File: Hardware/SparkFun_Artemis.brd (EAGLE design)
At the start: 15 x 10 mm, 74 parts, among them J1 PAD.4X.6, J10 PAD.4X.6, J11 PAD.4X.6, J12 PAD.4X.6, J13 PAD.4X.6, J14 PAD.4X.6, J15 PAD.4X.6, J16 PAD.4X.6, J17 PAD.4X.6, J18 PAD.4X.6, J19 PAD.4X.6, J2 PAD.4X.6, J20 PAD.4X.6, J21 PAD.4X.6, J22 PAD.4X.6, J23 PAD.4X.6, J24 PAD.4X.6, J25 PAD.4X.6, J26 PAD.4X.6, J27 PAD.4X.6, J28 PAD.4X.6, J29 PAD.4X.6, J3 PAD.4X.6, J30 PAD.4X.6, J31 PAD.4X.6, J32 PAD.4X.6, J34 PAD.4X.6, J35 PAD.4X.6, J36 PAD.4X.6, J37 PAD.4X.6, J38 PAD.4X.6, J39 PAD.4X.6, J4 PAD.4X.6, J40 PAD.4X.6, J41 PAD.4X.6, J42 PAD.4X.6, J43 PAD.4X.6, J44 PAD.4X.6, J45 PAD.4X.6, J46 PAD.35X.35, J47 PAD.4X.6, J48 PAD.4X.6, J49 PAD.4X.6, J5 PAD.4X.6, J6 PAD.4X.6, J7 PAD.4X.6, J8 PAD.4X.6, J9 PAD.4X.6, U1 AMBIQ-APOLLO3KBR, Y1 32MHz

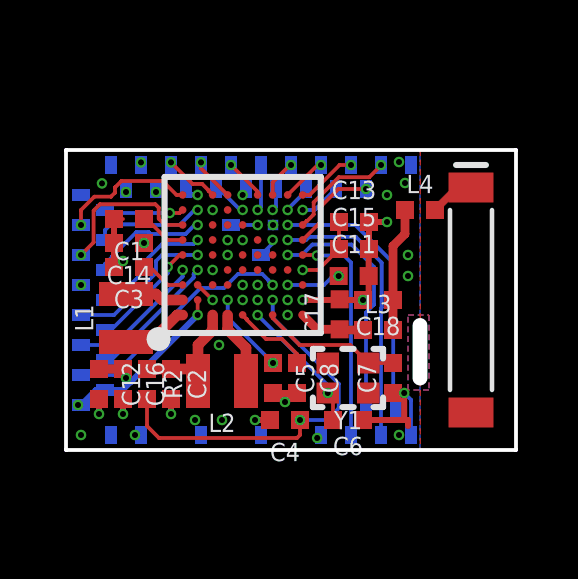
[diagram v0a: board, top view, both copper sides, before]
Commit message: Going to buried vias
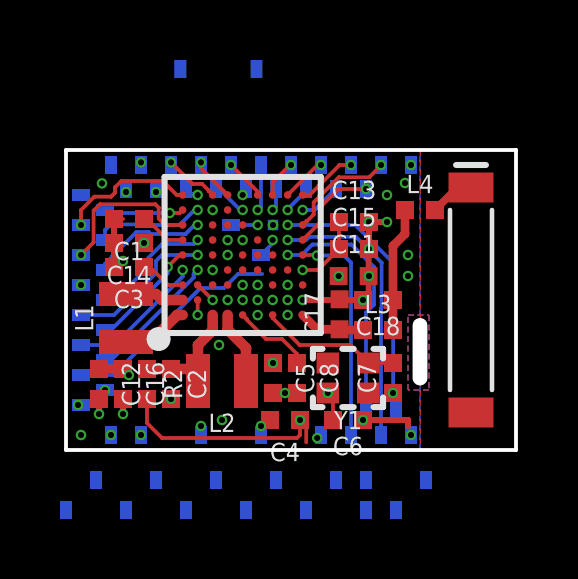
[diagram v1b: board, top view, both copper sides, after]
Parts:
- added J33, J50, J51, J52, J56, J57, J58, J59, J60, J61, J62, J63, J64, J65, J66, J67: PAD.4X.6, Module-Pads:MODULE_PAD
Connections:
- new net D0: J33.1, U1.H4
- new net D1: J50.1, U1.G4
- new net D14: J56.1, U1.D7
- new net D15: J57.1, U1.C7
- new net D16: J58.1, U1.D4
- new net D17: J59.1, U1.D3
- new net D18: J60.1, U1.C5
- new net D19: J61.1, U1.C3
- new net D2: J51.1, U1.F4
- new net D23: J62.1, U1.D8
- new net D3: J52.1, U1.G5
- new net D30: J63.1, U1.F6
- new net D34: J64.1, U1.C6
- new net D41: J65.1, U1.E5
- new net D45: J66.1, U1.F5
- new net D46: J67.1, U1.E7
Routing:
- net VDD: track 9.78 -> 4.13 mm, vias 7 -> 8
- net GND: track 15.7 -> 11.6 mm, vias 29 -> 34
- net VDCDCRF: track 12.7 -> 13.4 mm
- net N$3: track 4.84 -> 4.29 mm
- net !RST: track 7.96 -> 7.45 mm, vias 1 -> 0

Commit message: Buried via approach. Moar GPIOs!
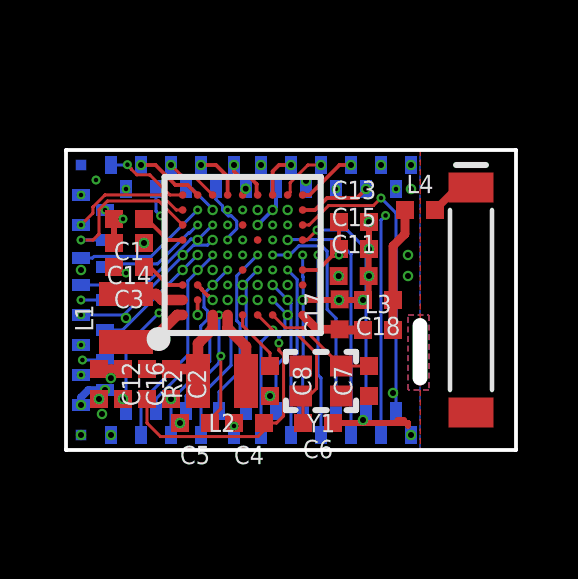
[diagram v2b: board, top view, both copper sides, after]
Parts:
- removed J34, J47, J48, J63, J67: PAD.4X.6, Module-Pads:MODULE_PAD
- J27, J44: value PAD.4X.6 -> PAD.35X.35; device Module-Pads:MODULE_PAD -> Module-Pads:MODULE_MINI_PAD
- J46: value PAD.35X.35 -> PAD.4X.6; device Module-Pads:MODULE_MINI_PAD -> Module-Pads:MODULE_PAD
- moved J56 11.4 mm to (2.00, 8.70), turned to 90 degrees
- moved J23 8.22 mm to (11.0, 1.30)
- moved J44 8.00 mm to (0.50, 0.50)
- moved J57 7.52 mm to (0.50, 5.50), turned to 0 degrees
- moved J36 7.40 mm to (10.0, 1.30)
- moved J30 6.61 mm to (7.00, 1.30), turned to 90 degrees
- moved J64 5.52 mm to (0.50, 4.50), turned to 180 degrees
- moved J4 5.47 mm to (4.00, 1.30), turned to 90 degrees
- moved J2 5.01 mm to (11.0, 8.70), turned to 270 degrees
- moved J33 4.74 mm to (7.50, 0.50)
- moved J66 4.53 mm to (5.10, 1.30)
- moved J18 4.50 mm to (0.50, 8.50), turned to 180 degrees
- moved J26 4.10 mm to (5.60, 0.50)
- moved J62 4.08 mm to (3.00, 8.70), turned to 90 degrees
- moved J51 3.86 mm to (6.00, 1.30)
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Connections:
- removed net D30: J63.1, U1.F6
- removed net D46: J67.1, U1.E7
- net GND: no longer J34.1, J47.1, J48.1
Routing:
- net D3: track 0.00 -> 7.46 mm, vias 0 -> 1
- net D18: track 0.00 -> 6.99 mm, vias 0 -> 1
- net D41: track 0.00 -> 6.58 mm, vias 0 -> 2
- net ~D44: track 3.74 -> 10.3 mm
- net SWDCK: track 0.66 -> 7.05 mm, vias 1 -> 2
- net D45: track 0.00 -> 5.97 mm, vias 0 -> 1
- net D1: track 0.00 -> 5.96 mm, vias 0 -> 2
- net D17: track 0.00 -> 5.94 mm, vias 0 -> 2
- net D19: track 0.00 -> 5.91 mm, vias 0 -> 2
- net D16: track 0.00 -> 5.79 mm, vias 0 -> 1
- net D0: track 0.00 -> 5.72 mm, vias 0 -> 1
- net D34: track 0.00 -> 5.42 mm, vias 0 -> 2
- net D15: track 0.00 -> 5.22 mm, vias 0 -> 1
- net ~D6: track 1.20 -> 6.25 mm, vias 1 -> 2
- net D2: track 0.00 -> 4.86 mm, vias 0 -> 1
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
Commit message: Commit for Quote
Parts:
- removed J60, J61, J62, J64, J65, J66: PAD.4X.6, Module-Pads:MODULE_PAD
- added J34, J47, J48, J53, J54, J55: PAD.4X.6, Module-Pads:MODULE_PAD
- J22, J38: value PAD.4X.6 -> PAD.35X.35; device Module-Pads:MODULE_PAD -> Module-Pads:MODULE_MINI_PAD
- J27, J44: value PAD.35X.35 -> PAD.4X.6; device Module-Pads:MODULE_MINI_PAD -> Module-Pads:MODULE_PAD
- moved J25 13.0 mm to (0.50, 7.50), turned to 0 degrees
- moved J23 12.7 mm to (0.50, 8.50), turned to 180 degrees
- moved J57 11.2 mm to (10.5, 0.50), turned to 270 degrees
- moved J56 10.9 mm to (10.0, 1.30), turned to 270 degrees
- moved J32 10.7 mm to (1.30, 4.00), turned to 0 degrees
- moved J24 10.3 mm to (1.30, 8.00), turned to 0 degrees
- moved J9 9.90 mm to (7.50, 9.50), turned to 90 degrees
- moved J5 9.87 mm to (9.50, 9.50), turned to 270 degrees
- moved J4 9.53 mm to (10.0, 8.70), turned to 270 degrees
- moved J43 9.35 mm to (3.50, 0.50)
- moved J41 9.22 mm to (2.50, 0.50)
- moved J22 9.00 mm to (0.50, 9.50), turned to 90 degrees
- moved J38 9.00 mm to (0.50, 0.50), turned to 0 degrees
- moved J39 9.00 mm to (1.50, 0.50), turned to 90 degrees
- moved J42 8.92 mm to (3.00, 1.30)
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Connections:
- net !RST: now also J50.1; no longer J30.1
- net BOOTLOAD: now also J7.1; no longer J3.1
- net D0: now also J51.1; no longer J33.1
- net D1: now also J49.1; no longer J50.1
- net D10: now also J8.1; no longer J43.1
- net D14: now also J20.1; no longer J56.1
- net D15: now also J29.1; no longer J57.1
- net D16: now also J42.1; no longer J58.1
- net D17: now also J43.1; no longer J59.1
- net D18: now also J41.1; no longer J60.1
- net D19: now also J40.1; no longer J61.1
- net D2: now also J48.1; no longer J51.1
- net D23: now also J18.1; no longer J62.1
- net D3: now also J54.1; no longer J52.1
- net D34: now also J31.1; no longer J64.1
- net D36: now also J55.1; no longer J38.1
- net D38: now also J56.1; no longer J36.1
- net D40: now also J5.1; no longer J22.1
- net D41: now also J45.1; no longer J65.1
- net D45: now also J46.1; no longer J66.1
- net D7: now also J13.1; no longer J19.1
- net D8: now also J11.1; no longer J42.1
- net D9: now also J6.1; no longer J46.1
- net GND: now also J1.1, J22.1, J38.1, J39.1, J47.1, J59.1; no longer J24.1, J25.1, J26.1, J27.1, J44.1, J45.1
- net RXI-0: now also J3.1; no longer J32.1
- net SWDIO: now also J10.1; no longer J1.1
- net TXO-0: now also J9.1; no longer J31.1
- net VDD: now also J36.1, J37.1; no longer J29.1, J49.1
- net XI: now also J35.1; no longer J9.1
- net XO: now also J34.1; no longer J10.1
- net ~AD11: now also J32.1; no longer J5.1
- net ~AD12: now also J26.1; no longer J6.1
- net ~AD13: now also J28.1; no longer J7.1
- net ~AD29: now also J33.1; no longer J15.1
- net ~AD31: now also J44.1; no longer J4.1
- net ~AD32: now also J24.1; no longer J16.1
- net ~AD33/SWO: now also J30.1; no longer J28.1
- net ~AD35: now also J14.1; no longer J17.1
- net ~D22: now also J17.1; no longer J40.1
- net ~D24: now also J16.1; no longer J11.1
- net ~D25: now also J25.1; no longer J12.1
- net ~D26: now also J27.1; no longer J13.1
- net ~D27: now also J19.1; no longer J8.1
- net ~D28: now also J21.1; no longer J14.1
- net ~D37: now also J57.1; no longer J39.1
- net ~D39: now also J4.1; no longer J21.1
- net ~D4: now also J15.1; no longer J41.1
- net ~D42: now also J53.1; no longer J37.1
- net ~D43: now also J52.1; no longer J35.1
- net ~D44: now also J58.1; no longer J23.1
- net ~D5: now also J12.1; no longer J20.1
- net ~D6: now also J23.1; no longer J18.1
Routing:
- net SWDCK: track 7.05 -> 5.35 mm
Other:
- board text added: "49"
- board text added: "50"
- board text added: "51"
- board text added: "52"
- board text added: "53"
- board text added: "54"
- board text added: "55"
- board text added: "56"
- board text added: "57"
- board text added: "58"
- board text added: "59"

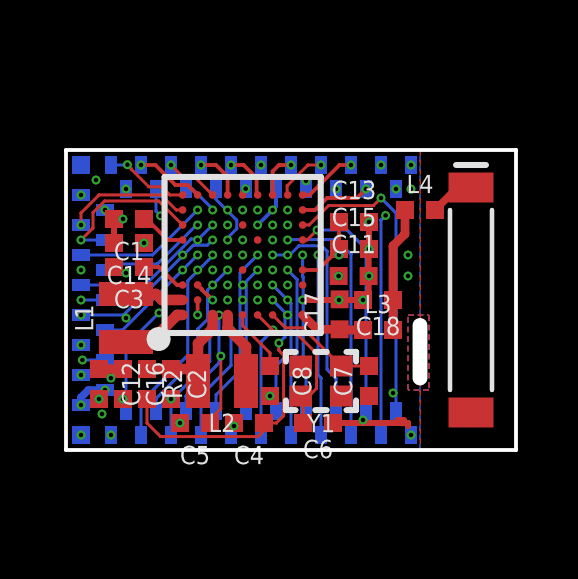
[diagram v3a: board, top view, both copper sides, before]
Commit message: Add fiducials. Add auto-bootload timing diagram.
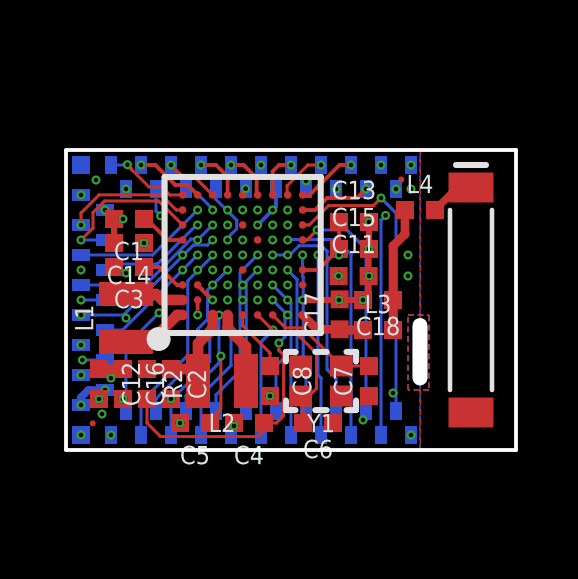
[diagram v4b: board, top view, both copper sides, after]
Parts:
- added FD3, FD4: FIDUCIAL0.2MM, SparkFun-Aesthetics:FIDUCIAL-0.2MM
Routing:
- net GND: track 9.65 -> 6.83 mm
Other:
- board text added: "RF Shield: H:1.2mm Thickness: 0.2mm"
- board text removed: "RF Shield: H:1.2mm Thickness: ~0.2mm"
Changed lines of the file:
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@@
 <setting verticaltext="up"/>
 </settings>
-<grid distance="0.05" unitdist="inch" unit="inch" style="lines" multiple="1" display="yes" altdistance="0.005" altunitdist="inch" altunit="inch"/>
+<grid distance="1" unitdist="mm" unit="mm" style="lines" multiple="1" display="yes" altdistance="0.1" altunitdist="mm" altunit="mm"/>
 <layers>
 <layer number="1" name="Top" color="4" fill="1" visible="yes" active="yes"/>
@@
 <layer number="27" name="tValues" color="7" fill="1" visible="no" active="yes"/>
 <layer number="28" name="bValues" color="7" fill="1" visible="no" active="yes"/>
-<layer number="29" name="tStop" color="7" fill="3" visible="no" active="yes"/>
+<layer number="29" name="tStop" color="7" fill="3" visible="yes" active="yes"/>
 <layer number="30" name="bStop" color="7" fill="6" visible="no" active="yes"/>
-<layer number="31" name="tCream" color="7" fill="4" visible="no" active="yes"/>
+<layer number="31" name="tCream" color="7" fill="4" visible="yes" active="yes"/>
 <layer number="32" name="bCream" color="7" fill="5" visible="no" active="yes"/>
 <layer number="33" name="tFinish" color="6" fill="3" visible="no" active="yes"/>
@@
 <layer number="46" name="Milling" color="12" fill="1" visible="no" active="yes"/>
 <layer number="47" name="Measures" color="7" fill="1" visible="no" active="yes"/>
-<layer number="48" name="RF_Shield2" color="63" fill="1" visible="no" active="yes"/>
+<layer number="48" name="RF_Shield2" color="63" fill="1" visible="yes" active="yes"/>
 <layer number="49" name="Reference" color="7" fill="1" visible="no" active="yes"/>
-<layer number="50" name="RF_Shield_Dimensions2" color="47" fill="1" visible="no" active="yes"/>
+<layer number="50" name="RF_Shield_Dimensions2" color="47" fill="1" visible="yes" active="yes"/>
 <layer number="51" name="tDocu" color="6" fill="1" visible="yes" active="yes"/>
-<layer number="52" name="bDocu" color="29" fill="1" visible="no" active="yes"/>
+<layer number="52" name="bDocu" color="29" fill="1" visible="yes" active="yes"/>
 <layer number="91" name="Nets" color="2" fill="1" visible="no" active="no"/>
 <layer number="92" name="Busses" color="1" fill="1" visible="no" active="no"/>
@@
 <text x="-2" y="19" size="0.9" layer="50" font="vector" ratio="15">RF Shield:
   H:1.2mm
-  Thickness: ~0.2mm
+  Thickness: 0.2mm
 </text>
 <dimension x1="11.8" y1="2.4" x2="11.8" y2="4.15" x3="16.2" y3="3.275" textsize="0.5" textratio="15" layer="50" dtype="horizontal" width="0.05"/>
@@
 <rectangle x1="1.8" y1="1" x2="2.2" y2="1.6" layer="52"/>
 <rectangle x1="10.8" y1="8.4" x2="11.2" y2="9" layer="52"/>
-<rectangle x1="0.325" y1="0.325" x2="0.675" y2="0.675" layer="52" rot="R180"/>
-<rectangle x1="0.325" y1="9.325" x2="0.675" y2="9.675" layer="52" rot="R180"/>
+<rectangle x1="0.198" y1="0.198" x2="0.802" y2="0.802" layer="52" rot="R180"/>
+<rectangle x1="0.198" y1="9.198" x2="0.802" y2="9.802" layer="52" rot="R180"/>
 <text x="10" y="8.7" size="0.2" layer="49" font="vector" ratio="15" align="center">4</text>
 <text x="3" y="8.7" size="0.2" layer="49" font="vector" ratio="15" align="center">18</text>
@@
 <text x="7.5" y="0.5" size="0.2" layer="49" font="vector" ratio="15" align="center">51</text>
 <text x="0.5" y="0.5" size="0.2" layer="49" font="vector" ratio="15" align="center">38</text>
+<wire x1="1" y1="0.4" x2="11" y2="0.4" width="0.2" layer="48"/>
 </plain>
 <attributes>
@@
 <element name="J46" library="Module-Pads" package="MODULE_PAD" value="PAD.4X.6" x="5" y="1.3" smashed="yes" rot="MR270"/>
 <element name="J47" library="Module-Pads" package="MODULE_PAD" value="PAD.4X.6" x="5.5" y="0.5" smashed="yes" rot="MR270"/>
+<element name="FD3" library="SparkFun-Aesthetics" package="FIDUCIAL-0.2MM" value="FIDUCIAL0.2MM" x="0.889" y="0.889" smashed="yes"/>
+<element name="FD4" library="SparkFun-Aesthetics" package="FIDUCIAL-0.2MM" value="FIDUCIAL0.2MM" x="11.176" y="9.017" smashed="yes"/>
 </elements>
 <signals>
@@
 <via x="10.1" y="7.6" extent="1-2" drill="0.15"/>
 <via x="9.9" y="5" extent="1-2" drill="0.15"/>
-<wire x1="11.4" y1="0.8" x2="11.4" y2="0.9" width="0.2" layer="1"/>
-<wire x1="8.9" y1="0.9" x2="11.4" y2="0.9" width="0.2" layer="1"/>
-<wire x1="11.049" y1="1" x2="11.273" y2="1" width="0.2" layer="1"/>
 <polygon width="0.1016" layer="1" isolate="0.127">
 <vertex x="11.808" y="10"/>
